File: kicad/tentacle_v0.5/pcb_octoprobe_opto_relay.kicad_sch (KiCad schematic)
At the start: 5 parts, among them U1101 GAQY221S

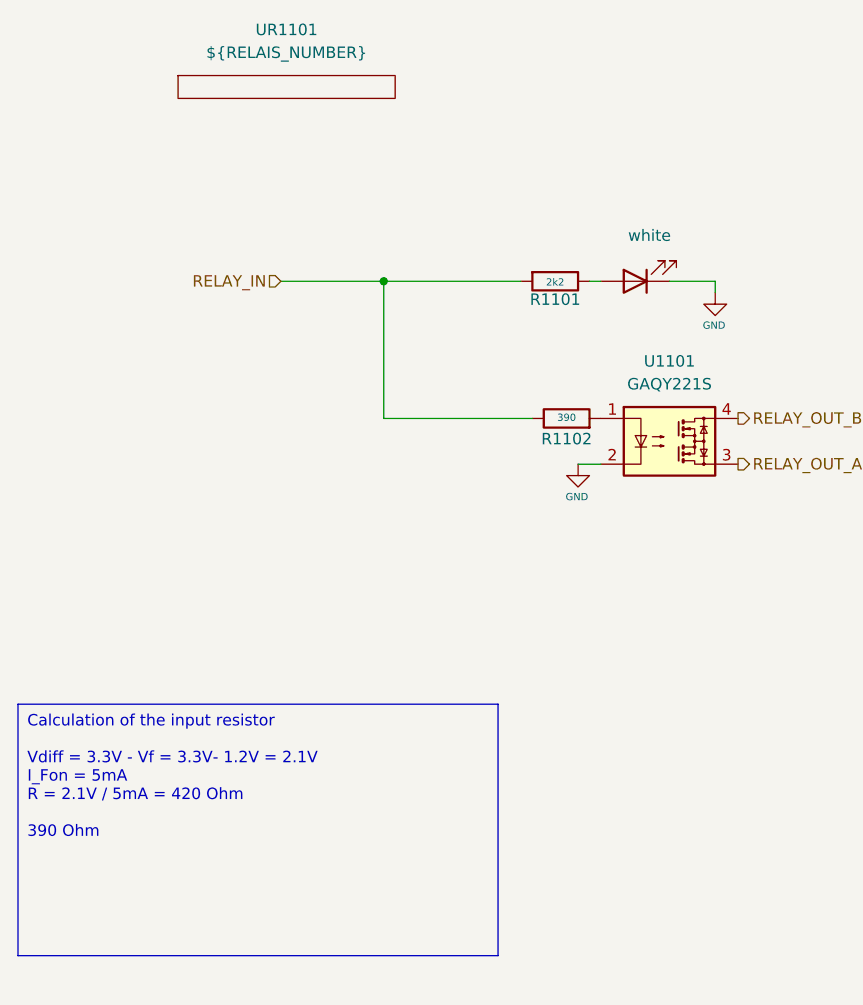
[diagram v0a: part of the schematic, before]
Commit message: Schematics: Fix ERC warnings
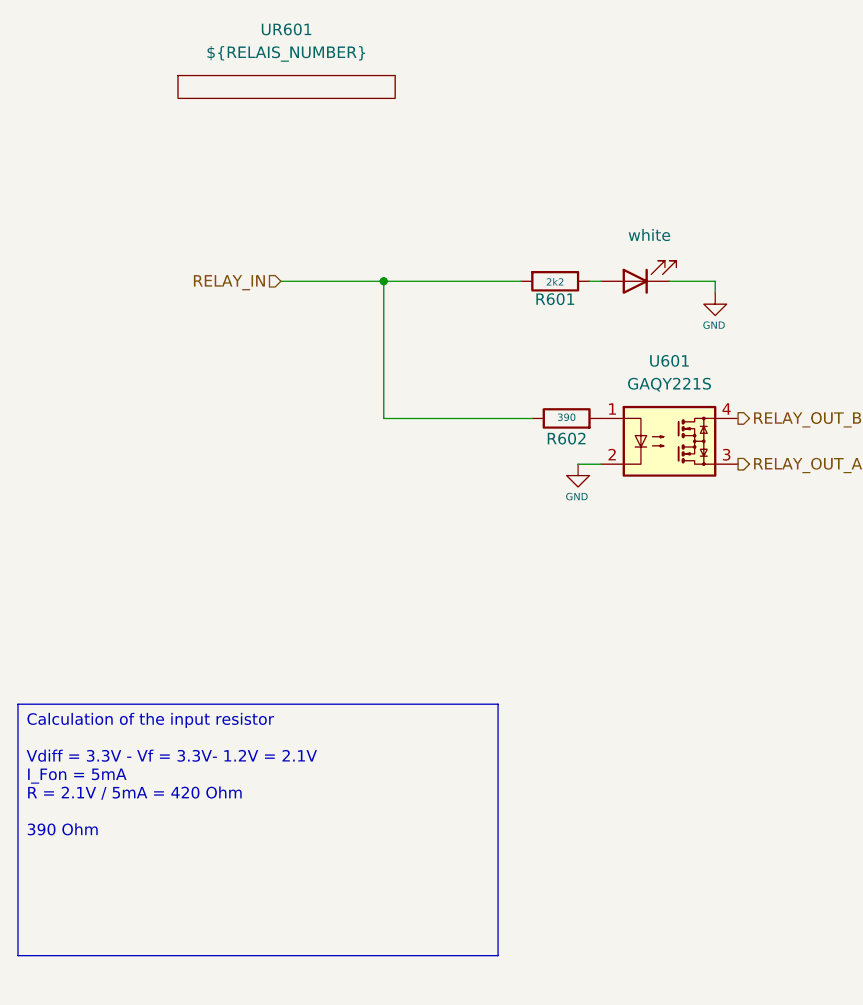
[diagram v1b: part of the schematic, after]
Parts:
- renumbered D1101 to D601, R1101 to R601, R1102 to R602, U1101 to U601, UR1101 to UR601
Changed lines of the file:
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@@
 (kicad_sch
-	(version 20231120)
+	(version 20250114)
 	(generator "eeschema")
-	(generator_version "8.0")
+	(generator_version "9.0")
 	(paper "A4")
 	(title_block
@@
 		(comment 1 "The MIT License (MIT)")
 	)
+	(text_box "Calculation of the input resistor\n\nVdiff = 3.3V - Vf = 3.3V- 1.2V = 2.1V\nI_Fon = 5mA\nR = 2.1V / 5mA = 420 Ohm\n\n390 Ohm"
+		(exclude_from_sim no)
+		(at 31.75 96.52 0)
+		(size 53.34 27.94)
+		(margins 0.9525 0.9525 0.9525 0.9525)
+		(stroke
+			(width 0)
+			(type default)
+		)
+		(fill
+			(type none)
+		)
+		(effects
+			(font
+				(size 1.27 1.27)
+			)
+			(justify left top)
+		)
+	)
 	(junction
 		(at 72.39 49.53)
@@
 			(width 0)
 			(type default)
-		)
-	)
-	(text_box "Calculation of the input resistor\n\nVdiff = 3.3V - Vf = 3.3V- 1.2V = 2.1V\nI_Fon = 5mA\nR = 2.1V / 5mA = 420 Ohm\n\n390 Ohm"
-		(exclude_from_sim no)
-		(at 31.75 96.52 0)
-		(size 53.34 27.94)
-		(stroke
-			(width 0)
-			(type default)
-		)
-		(fill
-			(type none)
-		)
-		(effects
-			(font
-				(size 1.27 1.27)
-			)
-			(justify left top)
 		)
 	)
@@
 		(on_board yes)
 		(dnp no)
-		(property "Reference" "R1102"
+		(property "Reference" "R602"
 			(at 92.71 67.056 90)
 			(effects
@@
 		(on_board yes)
 		(dnp no)
-		(property "Reference" "R1101"
+		(property "Reference" "R601"
 			(at 91.44 51.562 90)
 			(effects
@@
 		(dnp no)
 		(fields_autoplaced yes)
-		(property "Reference" "UR1101"
+		(property "Reference" "UR601"
 			(at 61.595 21.59 0)
 			(effects
@@
 		(dnp no)
 		(fields_autoplaced yes)
-		(property "Reference" "D1101"
+		(property "Reference" "D601"
 			(at 101.9175 42.545 0)
 			(effects
@@
 		(dnp no)
 		(fields_autoplaced yes)
-		(property "Reference" "#SYM1101"
+		(property "Reference" "#SYM601"
 			(at 274.32 167.005 0)
 			(effects
@@
 		(dnp no)
 		(fields_autoplaced yes)
-		(property "Reference" "U1101"
+		(property "Reference" "U601"
 			(at 104.14 58.42 0)
 			(effects
@@
 		(on_board yes)
 		(dnp no)
-		(property "Reference" "#PWR01102"
+		(property "Reference" "#PWR0602"
 			(at 109.22 57.15 0)
 			(effects
@@
 		(on_board yes)
 		(dnp no)
-		(property "Reference" "#PWR01101"
+		(property "Reference" "#PWR0601"
 			(at 93.98 76.2 0)
 			(effects
